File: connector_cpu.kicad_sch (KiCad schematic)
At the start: 25 parts, among them J201 Conn_ARM_JTAG_SWD_10, J202 Conn_02x10_Row_Letter_First, U201 STM32F302CBTx, U202 CAT24C32, U203 TLV73333PQDBVRQ1, U204 USBLC6-2SC6, Y201 8MHz / 20pF

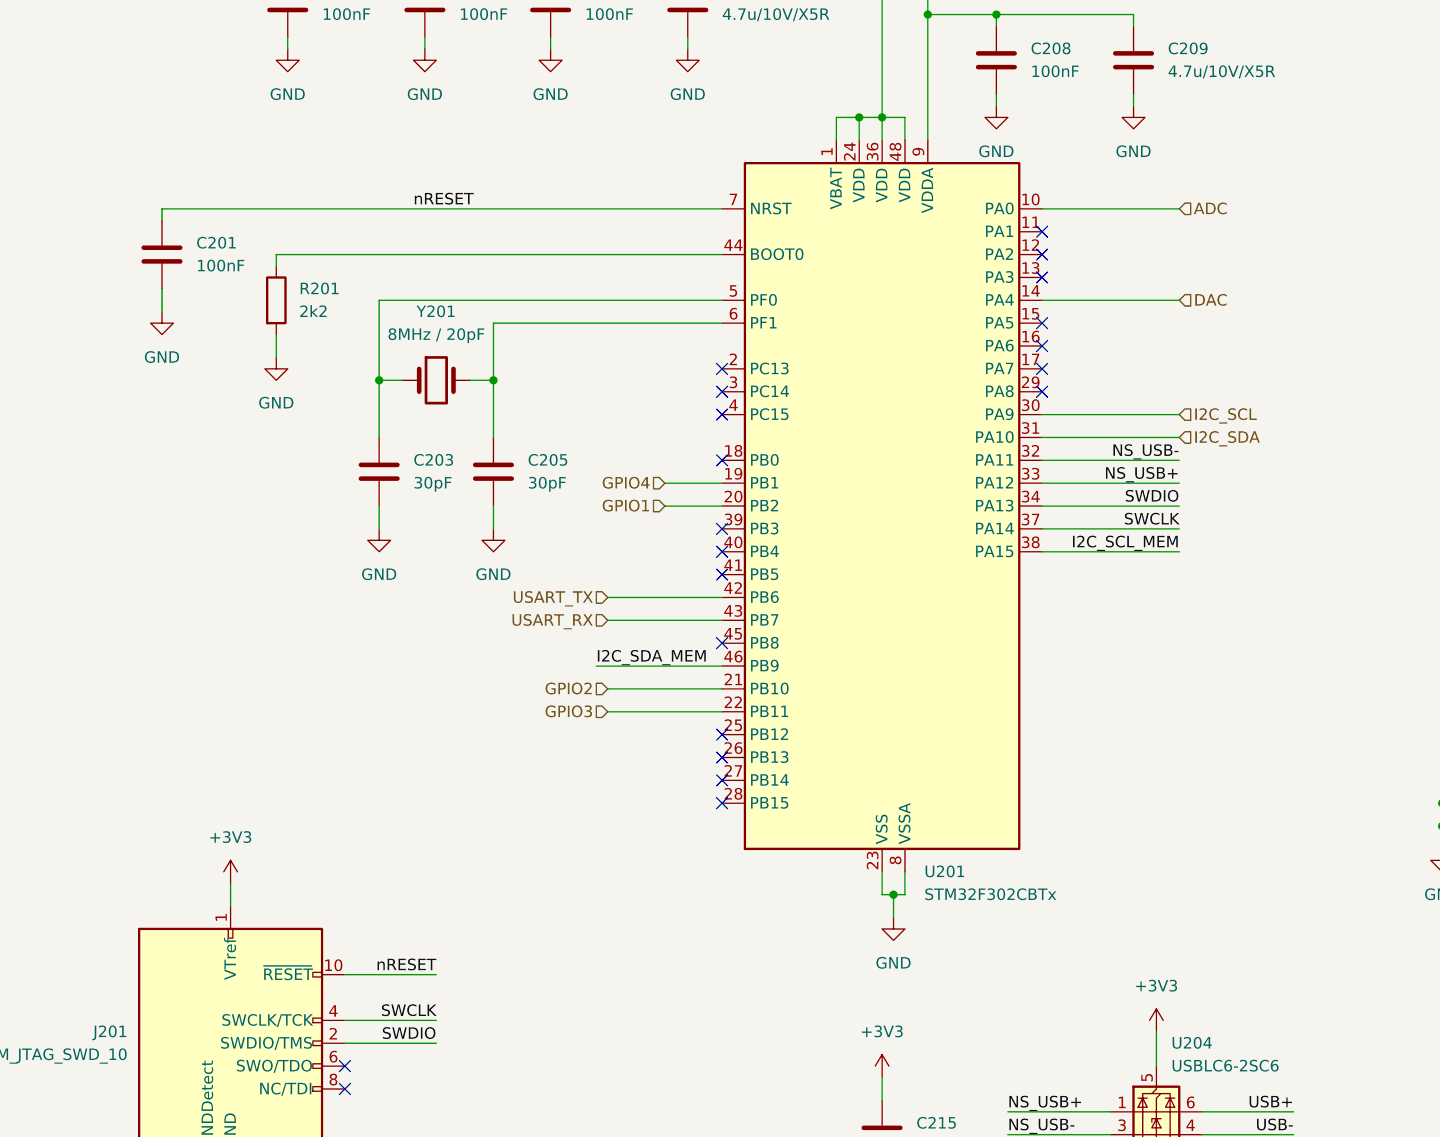
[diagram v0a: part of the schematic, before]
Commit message: update stm32, add some new 3d files
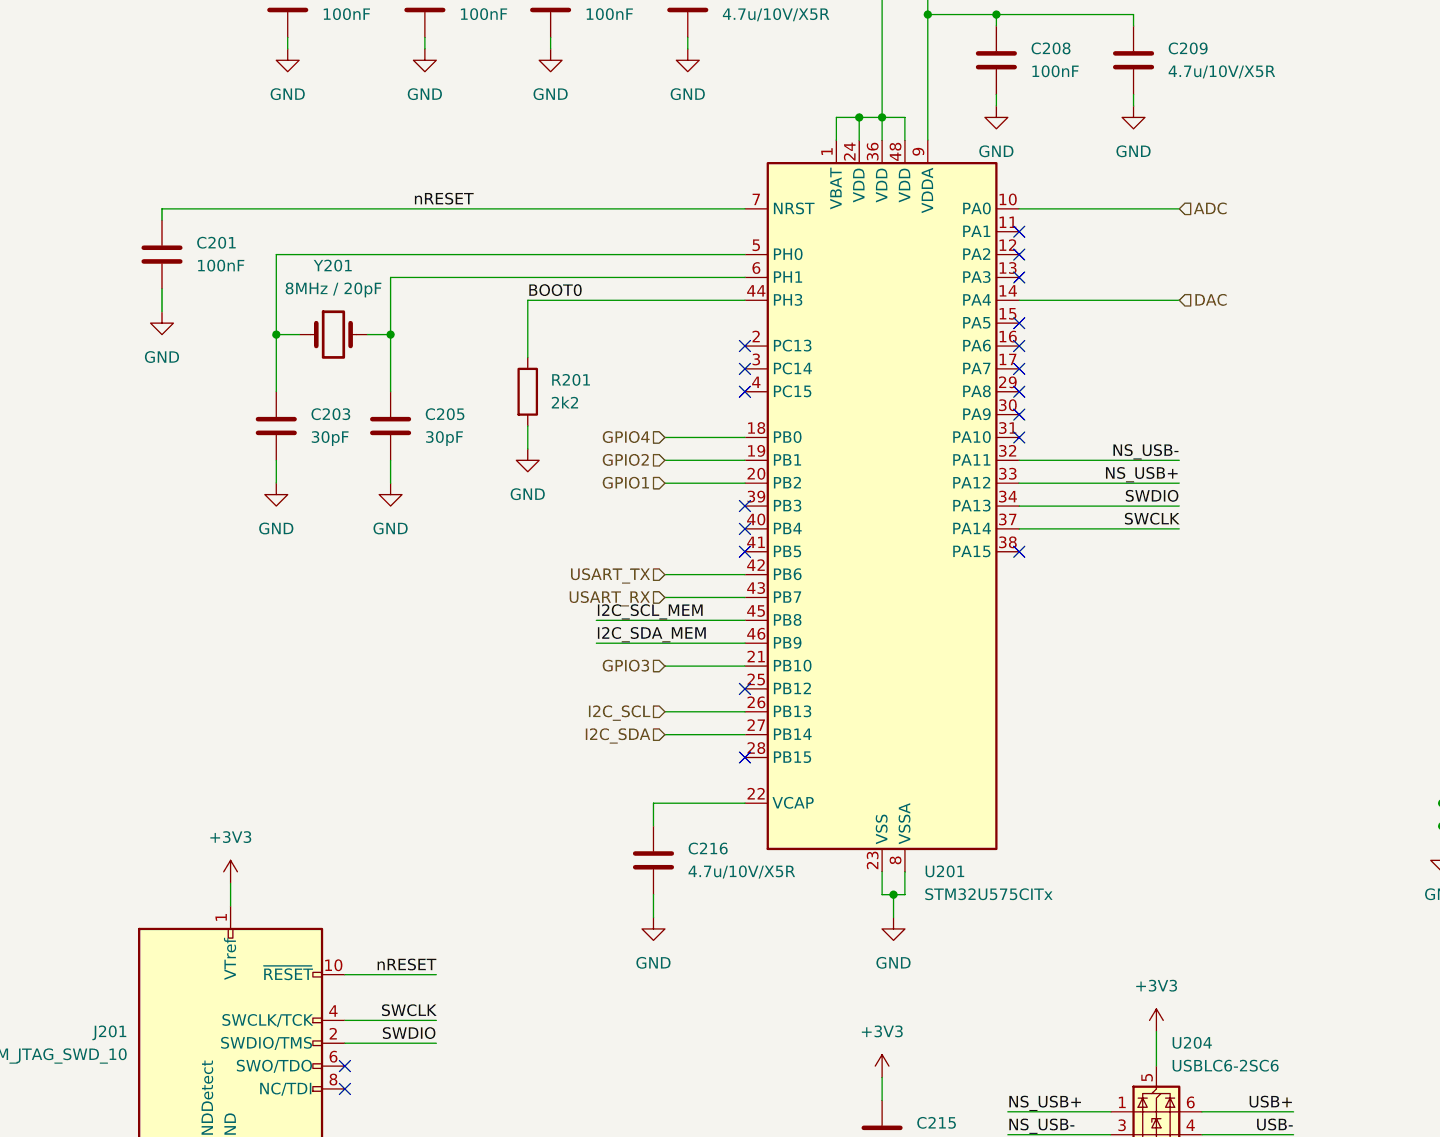
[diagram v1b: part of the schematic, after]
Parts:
- removed U201: STM32F302CBTx, Package_QFP:LQFP-48_7x7mm_P0.5mm, symbol MCU_ST_STM32F3:STM32F302CBTx
- added C216: 4.7u/10V/X5R, Capacitor_SMD:C_0805_2012Metric, symbol Device:C
- added U201: STM32U575CITx, Package_QFP:LQFP-48_7x7mm_P0.5mm, symbol MCU_ST_STM32U5:STM32U575CITx
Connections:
- net +3V3: now also U201.1 (VBAT), U201.24 (VDD), U201.36 (VDD), U201.48 (VDD), U201.9 (VDDA)
- net ADC: now also U201.10 (PA0)
- net DAC: now also U201.14 (PA4)
- net GND: now also C216.1, U201.23 (VSS), U201.35 (VSS), U201.47 (VSS), U201.8 (VSSA)
- net GPIO1: now also U201.20 (PB2)
- net GPIO2: now also U201.19 (PB1)
- net GPIO3: now also U201.21 (PB10)
- net GPIO4: now also U201.18 (PB0)
- net I2C_SCL: now also U201.26 (PB13)
- net I2C_SCL_MEM: now also U201.45 (PB8)
- net I2C_SDA: now also U201.27 (PB14)
- net I2C_SDA_MEM: now also U201.46 (PB9)
- net NS_USB+: now also U201.33 (PA12)
- net NS_USB-: now also U201.32 (PA11)
- net SWCLK: now also U201.37 (PA14)
- net SWDIO: now also U201.34 (PA13)
- net USART_RX: now also U201.43 (PB7)
- net USART_TX: now also U201.42 (PB6)
- net nRESET: now also U201.7 (NRST)
- net BOOT0: now reaches R201.1
- net BOOT0: now also U201.44 (PH3)
- net at C203.1, Y201.1: now also U201.5 (PH0)
- net at C205.1, Y201.2: now also U201.6 (PH1)
- new net: C216.2, U201.22 (VCAP)
- no-connect marks 27 -> 26
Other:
- moved on the sheet: C203, C205, R201, Y201

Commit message: add mouser part numbers
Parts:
- U201: MOUSER (none) -> 511-STM32U575CIT6

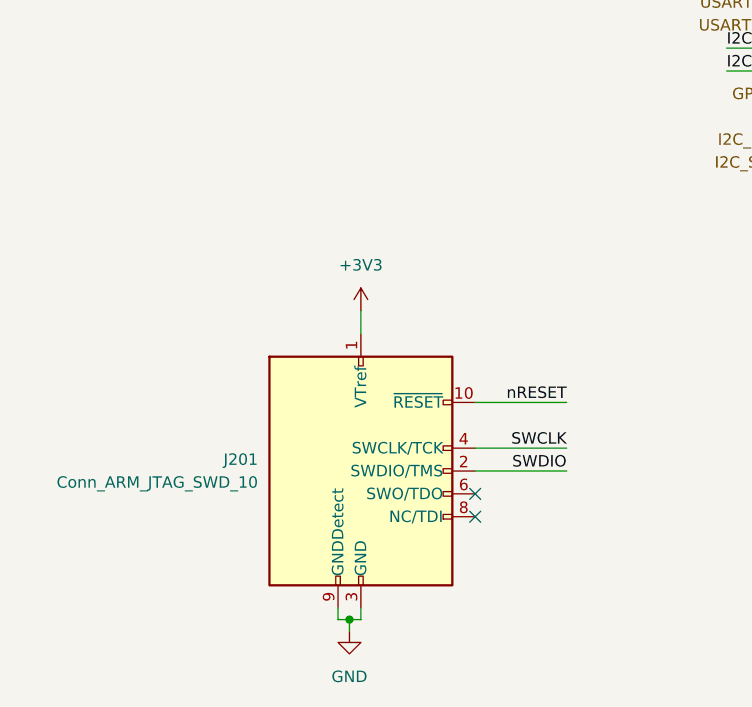
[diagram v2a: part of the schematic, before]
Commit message: Fix transistor symbol visibility and update polyline coordinates in schematic
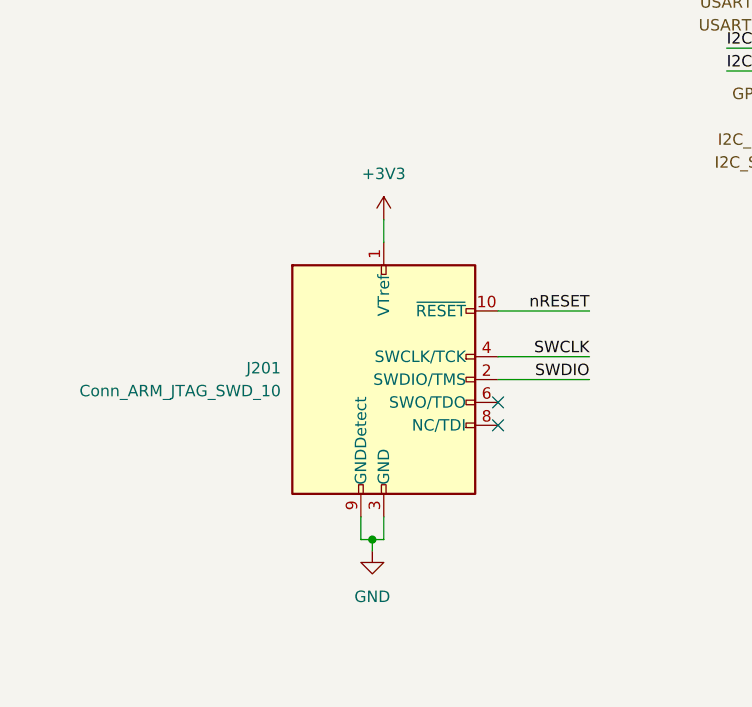
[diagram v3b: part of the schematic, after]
